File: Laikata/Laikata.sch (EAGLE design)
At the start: 19 parts, among them IC1_3V3 REG1117, IC2_5V REG1117, U1 S25FL127SABMFI101

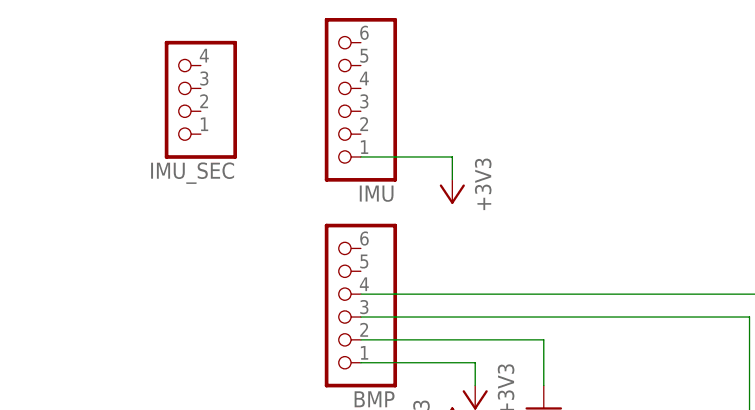
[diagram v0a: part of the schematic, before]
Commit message: IMU component
Created and added a custom component for the BNO055 sensor
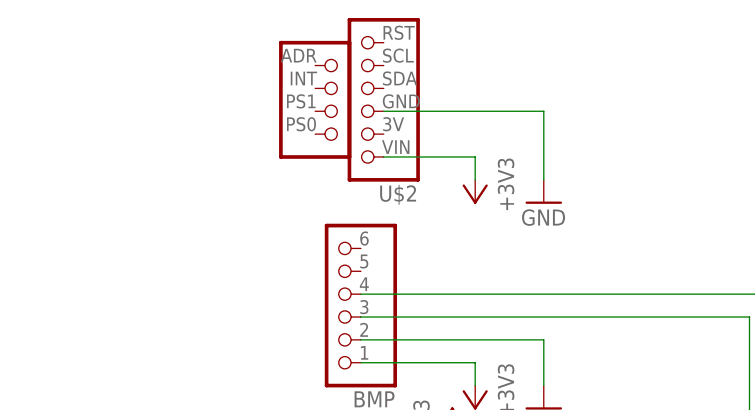
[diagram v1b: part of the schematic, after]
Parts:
- removed IMU: (no value), pinhead:PINHD-1X6
- removed IMU_SEC: (no value), pinhead:PINHD-1X4
- added U$2: IMU, hc12:IMU
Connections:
- net +3V3: now also U$2.VIN; no longer IMU.1
- net GND: now also U$2.GND
